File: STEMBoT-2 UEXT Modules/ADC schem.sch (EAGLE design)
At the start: 12 parts, among them IC3 8to3 Encoder

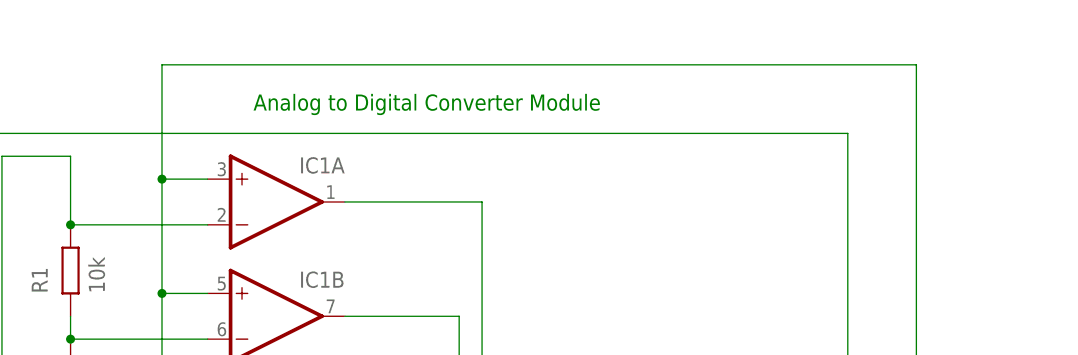
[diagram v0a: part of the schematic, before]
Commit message: Update ADC schem.sch
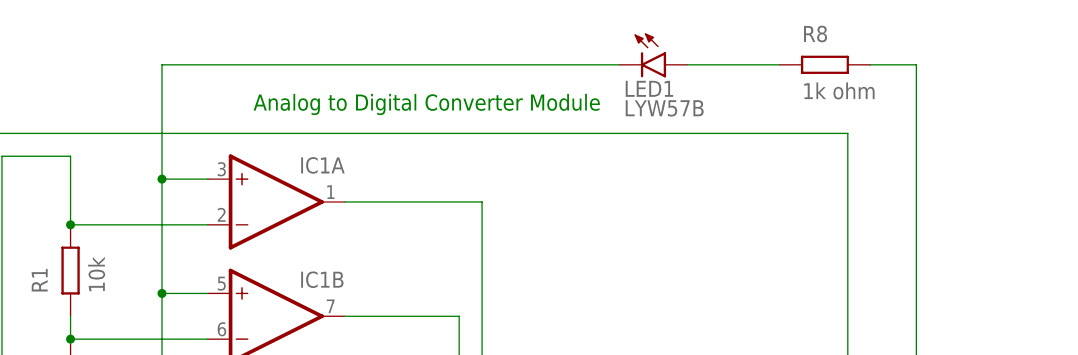
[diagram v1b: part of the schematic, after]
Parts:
- added LED1: LYW57B, led:LYW57B
- added R8: 1k ohm, ngspice-simulation:R
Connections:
- new net N$17: R8.2, X1-1.1
- new net N$18: LED1.A, R8.1
- net N$16: now also LED1.C; no longer X1-1.1
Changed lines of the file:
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@@
 <part name="X1" library="con-amp" library_urn="urn:adsk.eagle:library:127" deviceset="FSIDE-10" device="" package3d_urn="urn:adsk.eagle:package:8081495/1"/>
 <part name="3.5MMJACK" library="con-lumberg" library_urn="urn:adsk.eagle:library:163" deviceset="1503_04" device="" package3d_urn="urn:adsk.eagle:package:8553/1"/>
+<part name="LED1" library="led" library_urn="urn:adsk.eagle:library:259" deviceset="*W57B" device="" package3d_urn="urn:adsk.eagle:package:15859/1" technology="LY"/>
+<part name="R8" library="ngspice-simulation" library_urn="urn:adsk.eagle:library:527439" deviceset="R" device="" value="1k ohm"/>
 </parts>
 <sheets>
@@
 <attribute name="NAME" x="18.796" y="73.66" size="1.778" layer="95" rot="R90"/>
 <attribute name="VALUE" x="30.226" y="73.66" size="1.778" layer="96" rot="R90"/>
+</instance>
+<instance part="LED1" gate="G$1" x="111.76" y="109.22" smashed="yes" rot="R270">
+<attribute name="NAME" x="107.188" y="105.664" size="1.778" layer="95"/>
+<attribute name="VALUE" x="107.188" y="103.505" size="1.778" layer="96"/>
+</instance>
+<instance part="R8" gate="G$1" x="129.54" y="109.22" smashed="yes">
+<attribute name="NAME" x="127" y="111.76" size="1.778" layer="95"/>
+<attribute name="VALUE" x="127" y="105.41" size="1.778" layer="96"/>
 </instance>
 </instances>
@@
 <net name="N$16" class="0">
 <segment>
-<pinref part="X1" gate="-1" pin="1"/>
-<wire x1="144.78" y1="66.04" x2="139.7" y2="66.04" width="0.1524" layer="91"/>
-<wire x1="139.7" y1="66.04" x2="139.7" y2="109.22" width="0.1524" layer="91"/>
-<wire x1="139.7" y1="109.22" x2="55.88" y2="109.22" width="0.1524" layer="91"/>
 <wire x1="55.88" y1="109.22" x2="55.88" y2="96.52" width="0.1524" layer="91"/>
 <pinref part="IC2" gate="C" pin="+IN"/>
@@
 <wire x1="60.96" y1="96.52" x2="55.88" y2="96.52" width="0.1524" layer="91"/>
 <junction x="55.88" y="96.52"/>
+<pinref part="LED1" gate="G$1" pin="C"/>
+<wire x1="106.68" y1="109.22" x2="55.88" y2="109.22" width="0.1524" layer="91"/>
 </segment>
 </net>
@@
 </segment>
 </net>
+<net name="N$17" class="0">
+<segment>
+<pinref part="X1" gate="-1" pin="1"/>
+<wire x1="144.78" y1="66.04" x2="139.7" y2="66.04" width="0.1524" layer="91"/>
+<wire x1="139.7" y1="66.04" x2="139.7" y2="109.22" width="0.1524" layer="91"/>
+<pinref part="R8" gate="G$1" pin="2"/>
+<wire x1="134.62" y1="109.22" x2="139.7" y2="109.22" width="0.1524" layer="91"/>
+</segment>
+</net>
+<net name="N$18" class="0">
+<segment>
+<pinref part="R8" gate="G$1" pin="1"/>
+<pinref part="LED1" gate="G$1" pin="A"/>
+<wire x1="124.46" y1="109.22" x2="114.3" y2="109.22" width="0.1524" layer="91"/>
+</segment>
+</net>

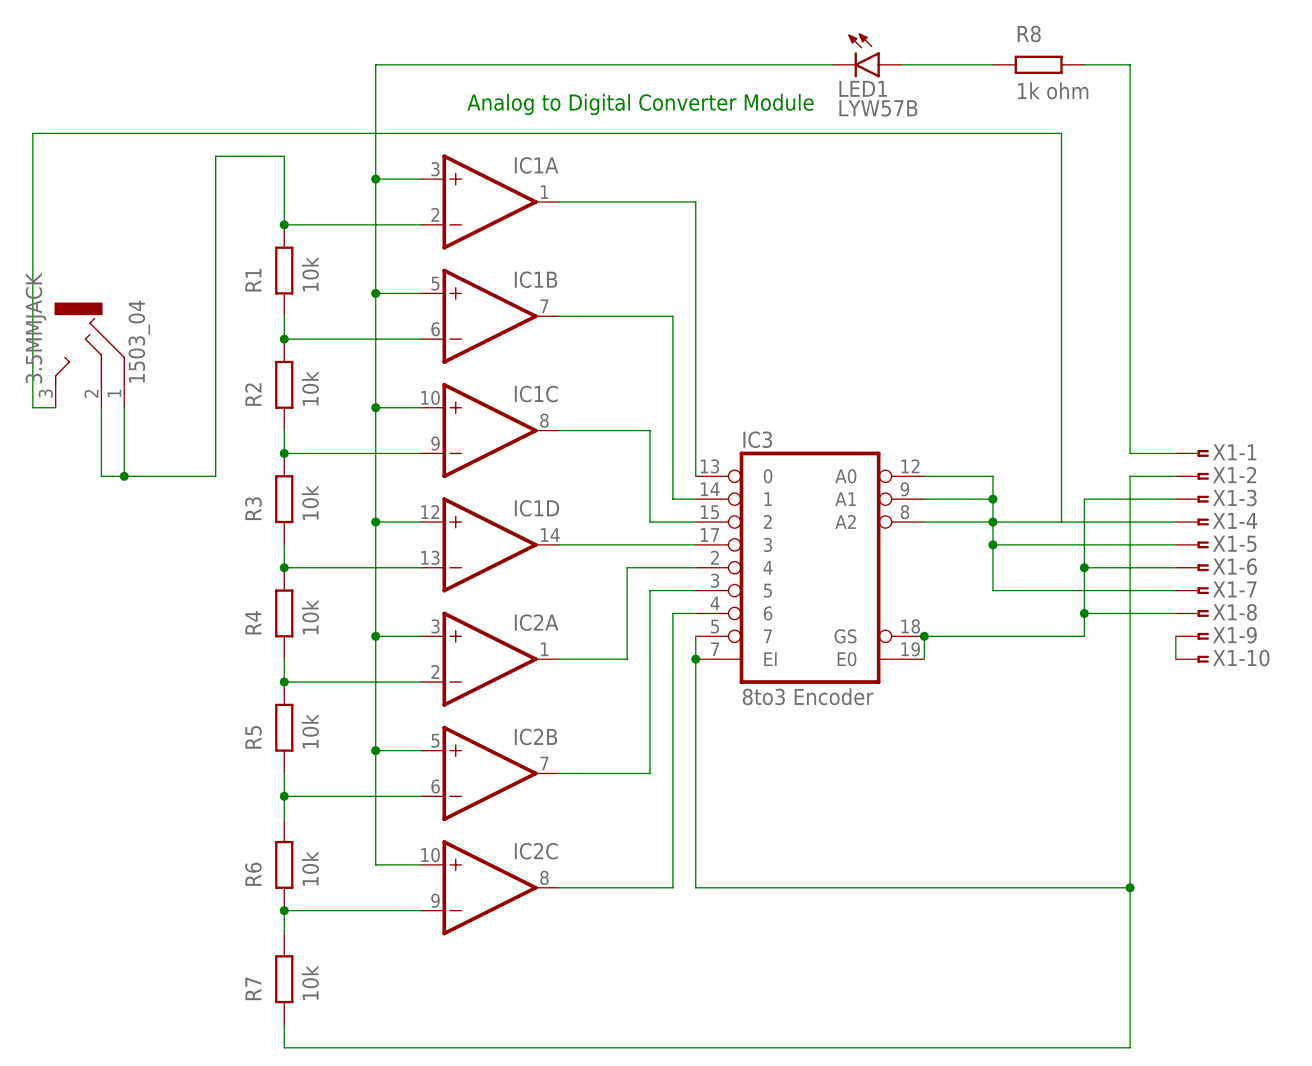
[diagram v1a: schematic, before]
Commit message: I am a little wary off all this stuff in here. I went ahead and added an ultrasonic schem in here. Dont know why it wasnt in before.
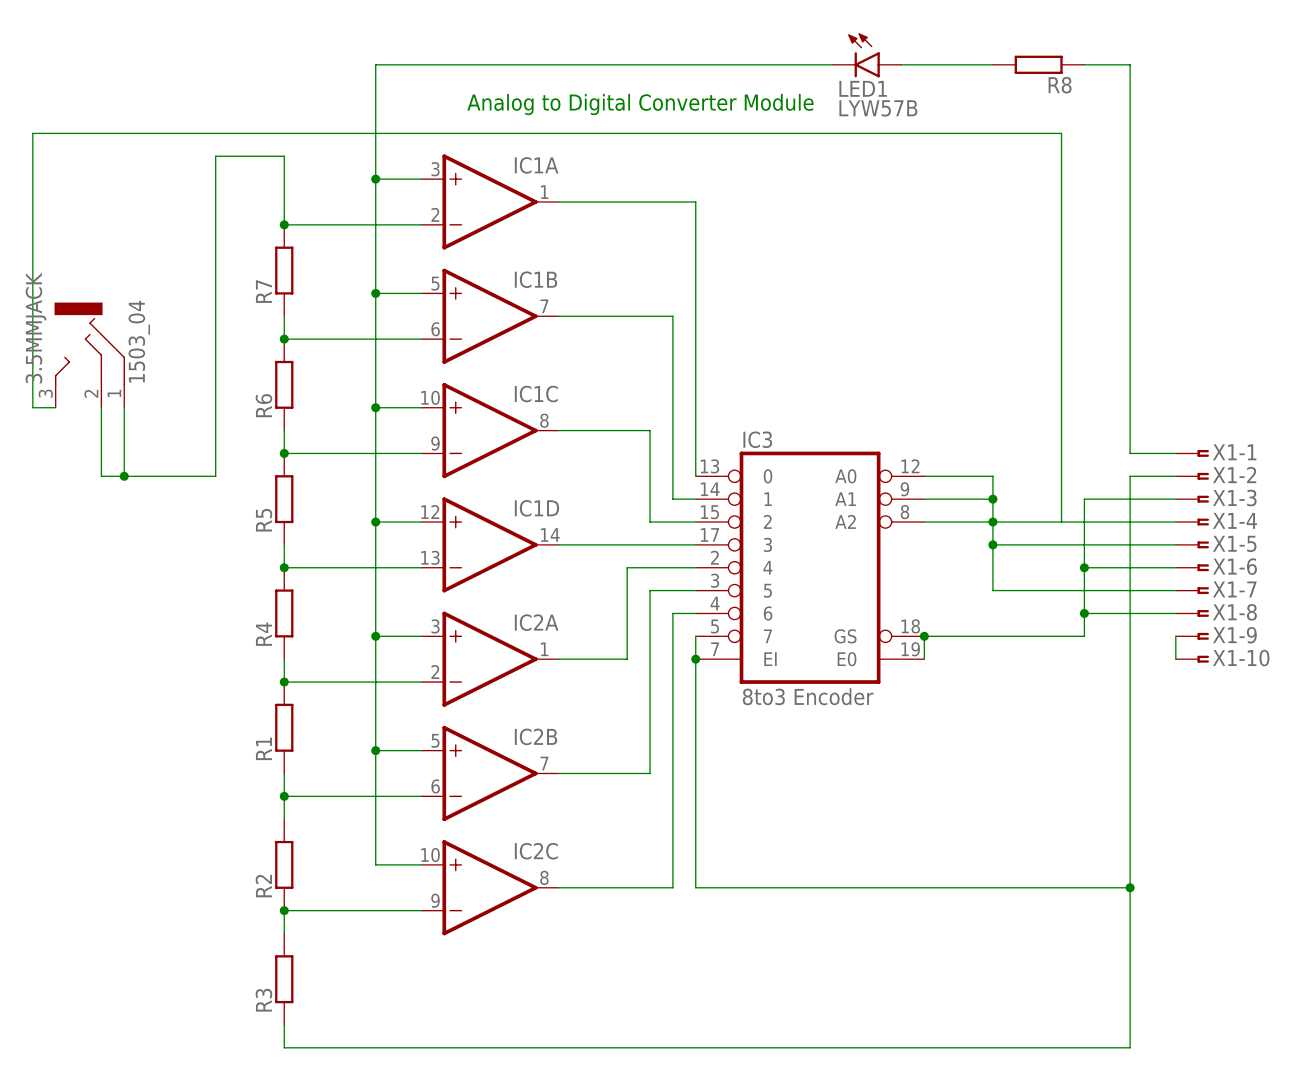
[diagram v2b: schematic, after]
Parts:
- R1, R2, R3, R4, R5, R6, R7: value 10k -> (none); device ngspice-simulation:R -> resistor-shunt:SMK
- R8: value 1k ohm -> (none); device ngspice-simulation:R -> resistor-shunt:SMK
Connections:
- net N$1: now also R6.1, R7.2; no longer R1.1, R2.2
- net N$15: now also R7.1; no longer R1.2
- net N$2: now also R5.1, R6.2; no longer R2.1, R3.2
- net N$3: now also R4.1, R5.2; no longer R3.1, R4.2
- net N$4: now also R1.1, R4.2; no longer R4.1, R5.2
- net N$5: now also R1.2, R2.1; no longer R5.1, R6.2
- net N$6: now also R2.2, R3.1; no longer R6.1, R7.2
- net N$7: now also R3.2; no longer R7.1
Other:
- moved on the sheet: R1, R2, R3, R5, R6, R7, R8
